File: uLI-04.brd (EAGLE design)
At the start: 57 x 38.5 mm, 39 parts, among them IC1 PIC18F14K50-I/SS, IC2 ADM2483, IC3 MCP130T, IC4 78L05F, J1 PICPROG2-V, J5 WEBP6-4, J6 WEBP6-4, J7 WEBP6-4, Q1 12.00 MHz, T1 IRF7306, X1 MINI-USB_SHIELD4P-USB-SPEC, X2 ARK1550/2_S

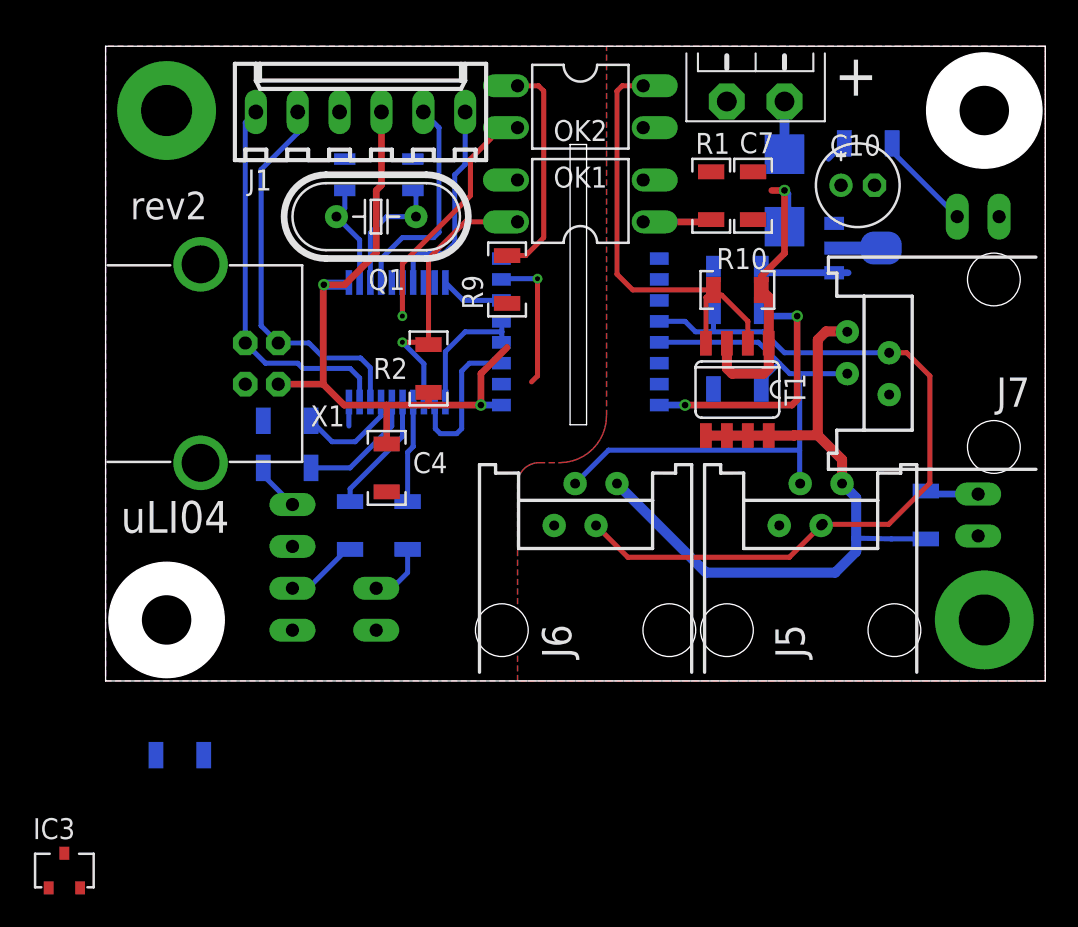
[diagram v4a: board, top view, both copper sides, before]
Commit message: Dokreslen rezistor 22 Ohm.
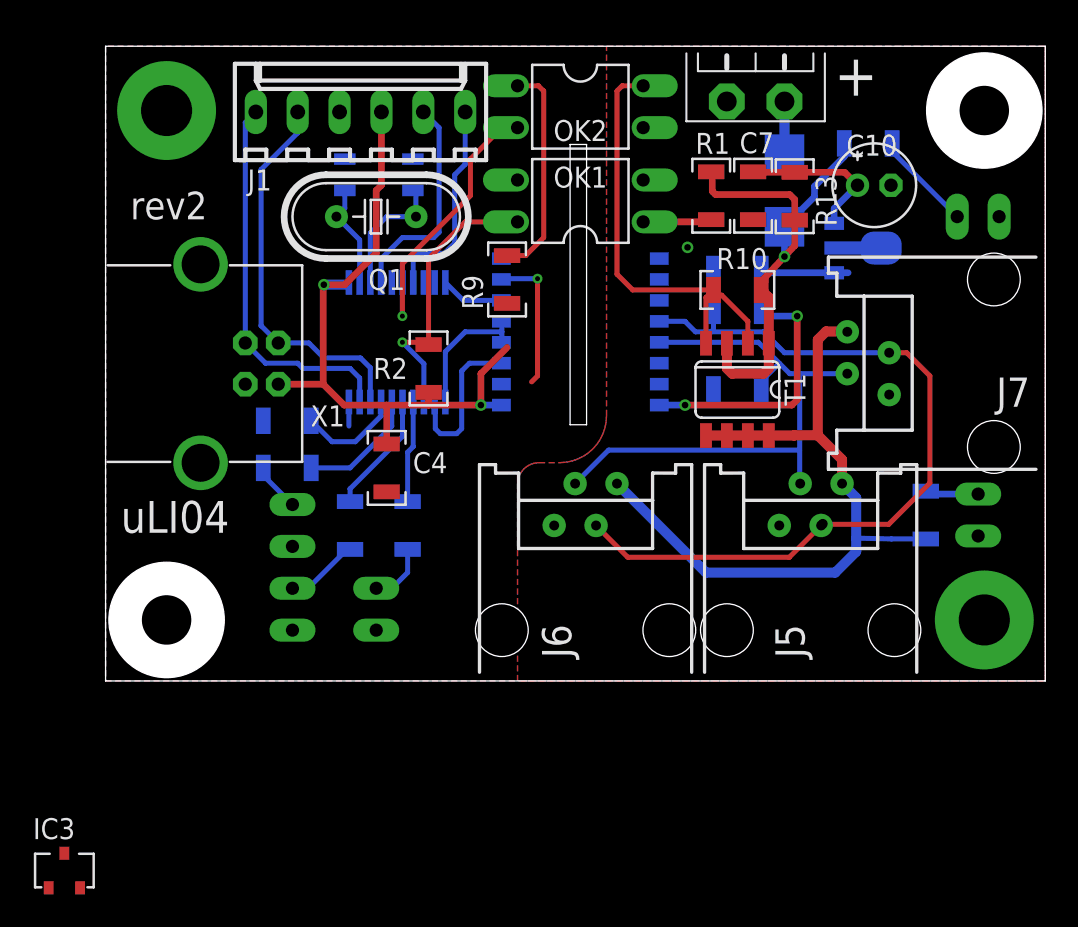
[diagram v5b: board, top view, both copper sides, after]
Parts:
- moved R13 50.4 mm to (43.8, 31.4), flipped to the top, turned to 270 degrees
- moved C10 1.00 mm to (48.6, 32.1)
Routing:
- net +12V: track 20.4 -> 30.4 mm
- net N$10: track 0.00 -> 9.57 mm
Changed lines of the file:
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@@
 <grid distance="0.5" unitdist="mm" unit="mm" style="dots" multiple="2" display="no" altdistance="0.1" altunitdist="mm" altunit="mm"/>
 <layers>
-<layer number="1" name="Top" color="3" fill="1" visible="yes" active="yes"/>
+<layer number="1" name="Top" color="3" fill="1" visible="no" active="yes"/>
 <layer number="2" name="Route2" color="1" fill="3" visible="no" active="no"/>
 <layer number="3" name="Route3" color="4" fill="3" visible="no" active="no"/>
@@
 <layer number="19" name="Unrouted" color="6" fill="1" visible="yes" active="yes"/>
 <layer number="20" name="Dimension" color="15" fill="1" visible="yes" active="yes"/>
-<layer number="21" name="tPlace" color="7" fill="1" visible="yes" active="yes"/>
+<layer number="21" name="tPlace" color="7" fill="1" visible="no" active="yes"/>
 <layer number="22" name="bPlace" color="7" fill="1" visible="yes" active="yes"/>
-<layer number="23" name="tOrigins" color="15" fill="1" visible="yes" active="yes"/>
+<layer number="23" name="tOrigins" color="15" fill="1" visible="no" active="yes"/>
 <layer number="24" name="bOrigins" color="15" fill="1" visible="yes" active="yes"/>
 <layer number="25" name="tNames" color="7" fill="1" visible="no" active="yes"/>
@@
 <layer number="44" name="Drills" color="7" fill="1" visible="no" active="yes"/>
 <layer number="45" name="Holes" color="7" fill="1" visible="no" active="yes"/>
-<layer number="46" name="Milling" color="3" fill="1" visible="yes" active="yes"/>
+<layer number="46" name="Milling" color="3" fill="1" visible="no" active="yes"/>
 <layer number="47" name="Measures" color="7" fill="1" visible="no" active="yes"/>
 <layer number="48" name="Document" color="7" fill="1" visible="no" active="yes"/>
-<layer number="49" name="Reference" color="7" fill="1" visible="yes" active="yes"/>
+<layer number="49" name="Reference" color="7" fill="1" visible="no" active="yes"/>
 <layer number="50" name="dxf" color="7" fill="1" visible="no" active="no"/>
-<layer number="51" name="tDocu" color="7" fill="1" visible="yes" active="yes"/>
+<layer number="51" name="tDocu" color="7" fill="1" visible="no" active="yes"/>
 <layer number="52" name="bDocu" color="7" fill="1" visible="yes" active="yes"/>
 <layer number="53" name="tGND_GNDA" color="7" fill="9" visible="no" active="no"/>
@@
 <element name="R10" library="rcl" package="R1206" value="100k" x="40.3225" y="25.7175"/>
 <element name="T1" library="transistor-fet" package="SO08-IRF" value="IRF7306" x="40.3225" y="19.685" rot="R180"/>
-<element name="C10" library="rcl" package="E2-5" value="10u/35V" x="47.625" y="32.0675" smashed="yes">
-<attribute name="NAME" x="45.927" y="33.8615" size="1.27" layer="25" ratio="10"/>
-<attribute name="VALUE" x="45.339" y="34.0195" size="1.27" layer="27" ratio="10"/>
+<element name="C10" library="rcl" package="E2-5" value="10u/35V" x="48.625" y="32.0675" smashed="yes">
+<attribute name="NAME" x="46.927" y="33.8615" size="1.27" layer="25" ratio="10"/>
+<attribute name="VALUE" x="46.339" y="34.0195" size="1.27" layer="27" ratio="10"/>
 </element>
 <element name="J5" library="con-malina" package="WEBP6-4_SHORT" value="WEBP6-4" x="44.7675" y="5.08" smashed="yes">
@@
 <attribute name="VALUE" x="50.2925" y="13.835" size="1.27" layer="28" font="vector" ratio="15" rot="MR270"/>
 </element>
-<element name="R13" library="rcl" package="R1206" value="22R" x="6.5" y="-2.5" rot="MR180"/>
+<element name="R13" library="rcl" package="R1206" value="22R" x="43.8" y="31.4" rot="R270"/>
 <element name="IC3" library="my" package="SOT23" value="MCP130T" x="-0.5" y="-9.5"/>
 </elements>
@@
 <contactref element="J7" pad="1"/>
 <contactref element="J5" pad="1"/>
+<via x="37.3" y="28.3" extent="1-16" drill="0.4"/>
 </signal>
 <signal name="VCCINT" class="1">
@@
 <contactref element="T1" pad="3"/>
 <contactref element="T1" pad="1"/>
-<wire x1="43.3865" y1="29.7565" x2="43.18" y2="29.55" width="0.6096" layer="16"/>
 <wire x1="39.6875" y1="22.485" x2="39.6875" y2="20.955" width="0.6096" layer="1"/>
 <wire x1="39.6875" y1="20.955" x2="40.005" y2="20.6375" width="0.6096" layer="1"/>
@@
 <wire x1="42.2275" y1="22.485" x2="42.2275" y2="25.2625" width="0.6096" layer="1"/>
 <wire x1="42.2275" y1="25.2625" x2="41.7725" y2="25.7175" width="0.6096" layer="1"/>
-<wire x1="43.3865" y1="29.7565" x2="43.3865" y2="31.5435" width="0.4064" layer="16"/>
-<wire x1="43.3865" y1="31.5435" x2="43.18" y2="31.75" width="0.4064" layer="16"/>
-<via x="43.18" y="31.75" extent="1-16" drill="0.4"/>
-<wire x1="43.18" y1="31.75" x2="42.4075" y2="31.75" width="0.4064" layer="1"/>
-<wire x1="41.7725" y1="25.7175" x2="41.7725" y2="26.5325" width="0.4064" layer="1"/>
-<wire x1="41.7725" y1="26.5325" x2="43.18" y2="27.94" width="0.4064" layer="1"/>
-<wire x1="43.18" y1="27.94" x2="43.18" y2="31.75" width="0.4064" layer="1"/>
-<wire x1="45.847" y1="33.6445" x2="46.81" y2="34.6075" width="0.3048" layer="16"/>
+<wire x1="41.7725" y1="25.7175" x2="41.7725" y2="26.2325" width="0.4064" layer="1"/>
 <contactref element="R13" pad="2"/>
-<wire x1="43.3865" y1="31.5435" x2="45.847" y2="33.6445" width="0" layer="19" extent="16-16"/>
-<wire x1="38.735" y1="32.8825" x2="42.4075" y2="31.75" width="0" layer="19" extent="1-1"/>
-<wire x1="7.95" y1="-2.5" x2="39.6875" y2="20.955" width="0" layer="19" extent="1-16"/>
+<wire x1="43.18" y1="29.55" x2="43.18" y2="27.74" width="0.4064" layer="16"/>
+<via x="43.18" y="27.74" extent="1-16" drill="0.4"/>
+<wire x1="43.18" y1="27.74" x2="41.7725" y2="26.2325" width="0.4064" layer="1"/>
+<wire x1="43.8" y1="29.95" x2="43.8" y2="28.4" width="0.4064" layer="1"/>
+<wire x1="43.8" y1="28.4" x2="43.18" y2="27.74" width="0.4064" layer="1"/>
+<wire x1="43.8" y1="29.95" x2="43.8" y2="31.2" width="0.4064" layer="1"/>
+<wire x1="43.8" y1="31.2" x2="43.5" y2="31.5" width="0.4064" layer="1"/>
+<wire x1="43.5" y1="31.5" x2="39" y2="31.5" width="0.4064" layer="1"/>
+<wire x1="39" y1="31.5" x2="38.8" y2="31.7" width="0.4064" layer="1"/>
+<wire x1="38.8" y1="31.7" x2="38.8" y2="32.8175" width="0.4064" layer="1"/>
+<wire x1="38.8" y1="32.8175" x2="38.735" y2="32.8825" width="0.4064" layer="1"/>
+<wire x1="46.81" y1="34.6075" x2="46.81" y2="33.81" width="0.4064" layer="16"/>
+<wire x1="46.81" y1="33.81" x2="45" y2="32" width="0.4064" layer="16"/>
+<wire x1="45" y1="32" x2="45" y2="31.37" width="0.4064" layer="16"/>
+<wire x1="45" y1="31.37" x2="43.18" y2="29.55" width="0.4064" layer="16"/>
 </signal>
 <signal name="XTAL2">
@@
 <contactref element="C7" pad="1"/>
 <contactref element="IC4" pad="3"/>
-<wire x1="46.1925" y1="29.7565" x2="46.609" y2="32.0675" width="0" layer="19" extent="16-16"/>
-<wire x1="41.275" y1="32.8825" x2="46.609" y2="32.0675" width="0" layer="19" extent="1-1"/>
-<wire x1="5.05" y1="-2.5" x2="41.275" y2="32.8825" width="0" layer="19" extent="1-16"/>
+<wire x1="46.1925" y1="29.7565" x2="46.1925" y2="30.651" width="0.4064" layer="16"/>
+<wire x1="46.1925" y1="30.651" x2="47.609" y2="32.0675" width="0.4064" layer="16"/>
+<wire x1="43.8" y1="32.85" x2="46.8265" y2="32.85" width="0.4064" layer="1"/>
+<wire x1="46.8265" y1="32.85" x2="47.609" y2="32.0675" width="0.4064" layer="1"/>
+<wire x1="43.8" y1="32.85" x2="41.3075" y2="32.85" width="0.4064" layer="1"/>
+<wire x1="41.3075" y1="32.85" x2="41.275" y2="32.8825" width="0.4064" layer="1"/>
 </signal>
 </signals>

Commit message: Dokreslen brown-down obvod do DPS.
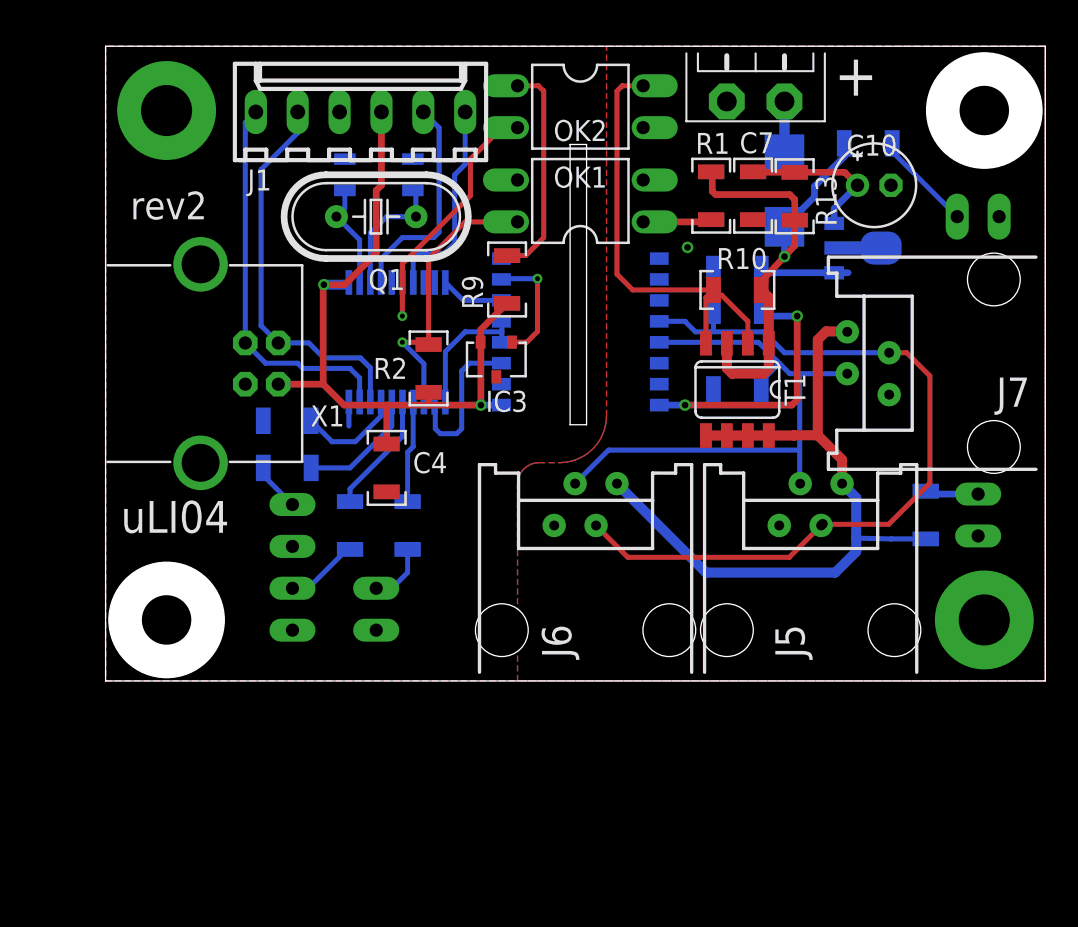
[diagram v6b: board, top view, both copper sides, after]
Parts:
- moved IC3 40.6 mm to (25.7, 21.5), turned to 180 degrees
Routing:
- net VDD: track 41.6 -> 44.3 mm
- net PV: track 8.62 -> 7.23 mm
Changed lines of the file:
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@@
 <grid distance="0.5" unitdist="mm" unit="mm" style="dots" multiple="2" display="no" altdistance="0.1" altunitdist="mm" altunit="mm"/>
 <layers>
-<layer number="1" name="Top" color="3" fill="1" visible="no" active="yes"/>
+<layer number="1" name="Top" color="3" fill="1" visible="yes" active="yes"/>
 <layer number="2" name="Route2" color="1" fill="3" visible="no" active="no"/>
 <layer number="3" name="Route3" color="4" fill="3" visible="no" active="no"/>
@@
 <layer number="19" name="Unrouted" color="6" fill="1" visible="yes" active="yes"/>
 <layer number="20" name="Dimension" color="15" fill="1" visible="yes" active="yes"/>
-<layer number="21" name="tPlace" color="7" fill="1" visible="no" active="yes"/>
+<layer number="21" name="tPlace" color="7" fill="1" visible="yes" active="yes"/>
 <layer number="22" name="bPlace" color="7" fill="1" visible="yes" active="yes"/>
-<layer number="23" name="tOrigins" color="15" fill="1" visible="no" active="yes"/>
+<layer number="23" name="tOrigins" color="15" fill="1" visible="yes" active="yes"/>
 <layer number="24" name="bOrigins" color="15" fill="1" visible="yes" active="yes"/>
 <layer number="25" name="tNames" color="7" fill="1" visible="no" active="yes"/>
@@
 <layer number="44" name="Drills" color="7" fill="1" visible="no" active="yes"/>
 <layer number="45" name="Holes" color="7" fill="1" visible="no" active="yes"/>
-<layer number="46" name="Milling" color="3" fill="1" visible="no" active="yes"/>
+<layer number="46" name="Milling" color="3" fill="1" visible="yes" active="yes"/>
 <layer number="47" name="Measures" color="7" fill="1" visible="no" active="yes"/>
 <layer number="48" name="Document" color="7" fill="1" visible="no" active="yes"/>
-<layer number="49" name="Reference" color="7" fill="1" visible="no" active="yes"/>
+<layer number="49" name="Reference" color="7" fill="1" visible="yes" active="yes"/>
 <layer number="50" name="dxf" color="7" fill="1" visible="no" active="no"/>
-<layer number="51" name="tDocu" color="7" fill="1" visible="no" active="yes"/>
+<layer number="51" name="tDocu" color="7" fill="1" visible="yes" active="yes"/>
 <layer number="52" name="bDocu" color="7" fill="1" visible="yes" active="yes"/>
 <layer number="53" name="tGND_GNDA" color="7" fill="9" visible="no" active="no"/>
@@
 </element>
 <element name="R13" library="rcl" package="R1206" value="22R" x="43.8" y="31.4" rot="R270"/>
-<element name="IC3" library="my" package="SOT23" value="MCP130T" x="-0.5" y="-9.5"/>
+<element name="IC3" library="my" package="SOT23" value="MCP130T" x="25.7" y="21.5" rot="R180"/>
 </elements>
 <signals>
@@
 <contactref element="IC2" pad="2"/>
 <contactref element="IC3" pad="3"/>
-<wire x1="13.335" y1="5.08" x2="-0.5" y2="-8.45" width="0" layer="19" extent="1-1"/>
 </signal>
 <signal name="VBUS">
@@
 <contactref element="IC2" pad="1"/>
 <contactref element="R9" pad="2"/>
-<wire x1="26.3525" y1="22.225" x2="24.765" y2="20.6375" width="0.4064" layer="1"/>
-<wire x1="24.765" y1="20.6375" x2="24.765" y2="18.7325" width="0.4064" layer="1"/>
 <contactref element="X1" pad="1"/>
 <wire x1="19.05" y1="18.7325" x2="16.4675" y2="18.7325" width="0.4064" layer="1"/>
@@
 <wire x1="16.4675" y1="18.7325" x2="15.2" y2="20" width="0.4064" layer="1"/>
 <contactref element="IC3" pad="2"/>
-<wire x1="26.3525" y1="22.225" x2="26.3525" y2="24.9025" width="0" layer="19" extent="1-1"/>
-<wire x1="0.45" y1="-10.55" x2="19.05" y2="16.3725" width="0" layer="19" extent="1-1"/>
+<wire x1="24.765" y1="18.7325" x2="24.765" y2="22.535" width="0.4064" layer="1"/>
+<wire x1="24.765" y1="22.535" x2="24.75" y2="22.55" width="0.4064" layer="1"/>
+<wire x1="24.75" y1="22.55" x2="24.75" y2="23.3" width="0.4064" layer="1"/>
+<wire x1="24.75" y1="23.3" x2="26.3525" y2="24.9025" width="0.4064" layer="1"/>
 </signal>
 <signal name="PROC_RX">
@@
 <signal name="PV">
 <contactref element="IC2" pad="7"/>
-<wire x1="27.84" y1="20.14" x2="28.2" y2="20.5" width="0.3048" layer="1"/>
-<wire x1="28.2" y1="20.5" x2="28.2" y2="26.4" width="0.3048" layer="1"/>
 <via x="28.2" y="26.4" extent="1-16" drill="0.3"/>
 <wire x1="28.2" y1="26.4" x2="26.0571" y2="26.4" width="0.3048" layer="16"/>
 <wire x1="26.0571" y1="26.4" x2="26.0096" y2="26.3525" width="0.3048" layer="16"/>
 <contactref element="IC3" pad="1"/>
-<wire x1="-1.45" y1="-10.55" x2="27.84" y2="20.14" width="0" layer="19" extent="1-1"/>
+<wire x1="26.65" y1="22.55" x2="27.55" y2="22.55" width="0.3048" layer="1"/>
+<wire x1="27.55" y1="22.55" x2="28.2" y2="23.2" width="0.3048" layer="1"/>
+<wire x1="28.2" y1="26.4" x2="28.2" y2="23.2" width="0.3048" layer="1"/>
 </signal>
 <signal name="N$5">

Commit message: Upravena hodnota kondenzatoru XN na 22uF.
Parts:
- C10: value 10u/35V -> 22u/25V
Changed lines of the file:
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@@
 <element name="R10" library="rcl" package="R1206" value="100k" x="40.3225" y="25.7175"/>
 <element name="T1" library="transistor-fet" package="SO08-IRF" value="IRF7306" x="40.3225" y="19.685" rot="R180"/>
-<element name="C10" library="rcl" package="E2-5" value="10u/35V" x="48.625" y="32.0675" smashed="yes">
+<element name="C10" library="rcl" package="E2-5" value="22u/25V" x="48.625" y="32.0675" smashed="yes">
 <attribute name="NAME" x="46.927" y="33.8615" size="1.27" layer="25" ratio="10"/>
 <attribute name="VALUE" x="46.339" y="34.0195" size="1.27" layer="27" ratio="10"/>
